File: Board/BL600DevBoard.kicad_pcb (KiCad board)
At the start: 2 copper layers, 42 parts, among them CN1 Socket_BL600, CON1 USB-MINI-B, P1 CONN_01X17, P2 CONN_BL600_SWDIF, P3 CONN_01X17, SW1 DIPSW_8, U1 93C56, U2 FT232H, U3 TC7SZ125, U4 TC7SZ125, X1 12M

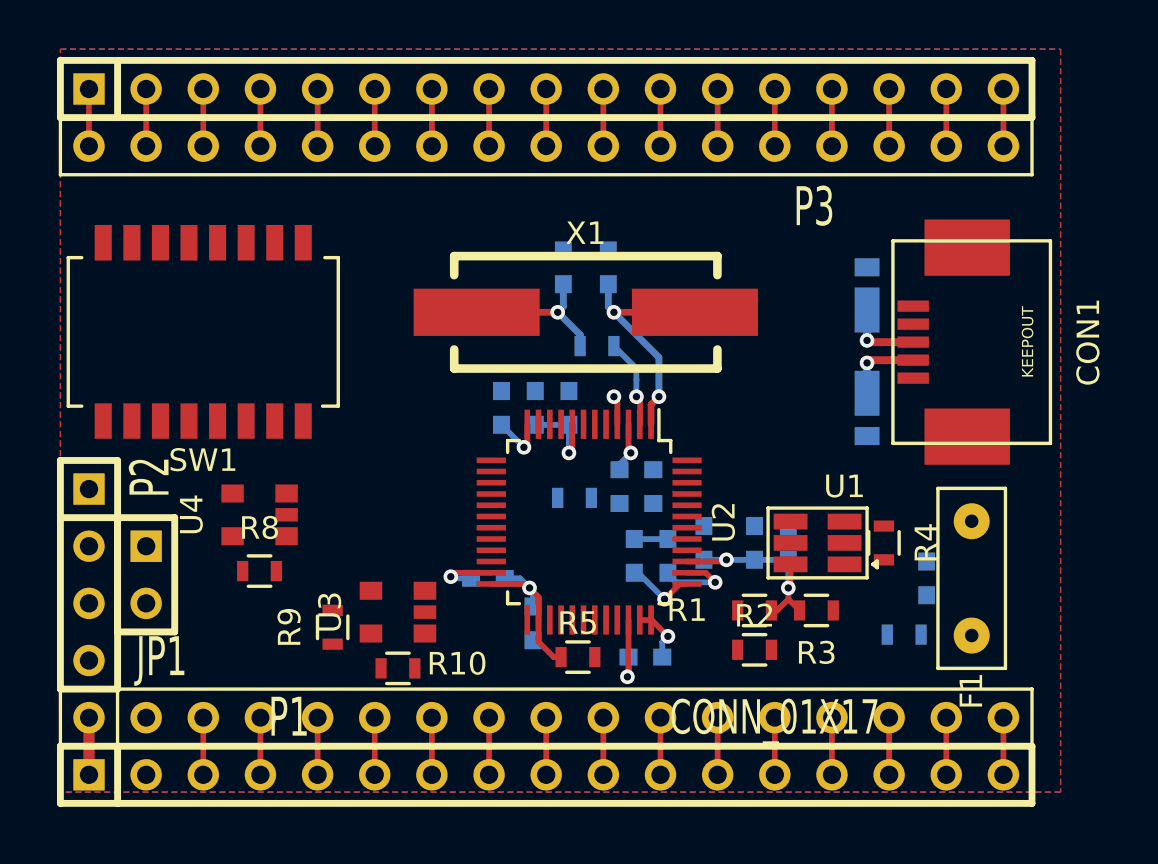
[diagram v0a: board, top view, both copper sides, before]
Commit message: Add panelized board cutting path data
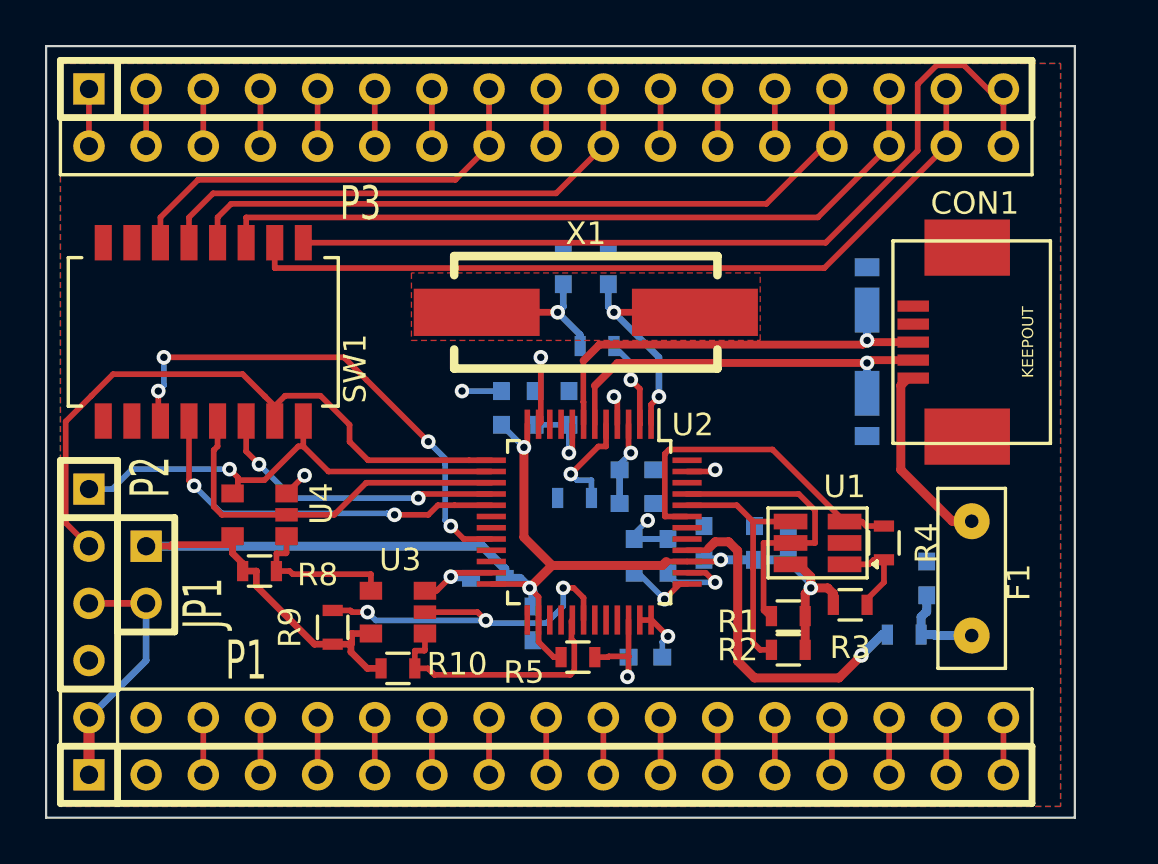
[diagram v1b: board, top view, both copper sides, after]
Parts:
- moved R1 1.52 mm to (184.8, 115.5)
- moved R3 1.52 mm to (187.5, 115.0)
- moved R2 1.50 mm to (184.8, 117.0)
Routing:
- net /VCC3.3: track 20.3 -> 69.9 mm
- net Net-(CN1-Pad18): track 2.54 -> 39.4 mm
- net Net-(CN1-Pad19): track 2.54 -> 35.8 mm
- net Net-(CN1-Pad20): track 2.54 -> 33.6 mm
- net Net-(CN1-Pad21): track 2.54 -> 32.4 mm
- net /SWDCLK_TxD: track 0.00 -> 28.9 mm
- net /RI#: track 0.00 -> 22.5 mm, vias 0 -> 4
- net /SWDIO_RxD: track 0.00 -> 21.4 mm, vias 0 -> 1
- net Net-(CN1-Pad25): track 2.54 -> 23.4 mm
- net Net-(CN1-Pad27): track 2.54 -> 19.6 mm
- net /TDO_RTS#: track 0.00 -> 17.0 mm
- net /DTR#: track 0.00 -> 16.9 mm, vias 0 -> 2
- net /SWDIO_OE: track 0.00 -> 16.5 mm, vias 0 -> 3
- net Net-(CON1-Pad3): track 3.43 -> 19.2 mm
- net Net-(FB1-Pad2): track 0.00 -> 15.2 mm, vias 0 -> 1
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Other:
- board outline added: 45.7 x 34.3 mm
- net class CLOCK: trace_width 0.3 -> 0.254
- net class POWER: trace_width 0.254 -> 0.35
- board text added: "BL600DevBoard Rev.A 20141112"

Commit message: TDI/TDO修正版に基板レイアウトを変更
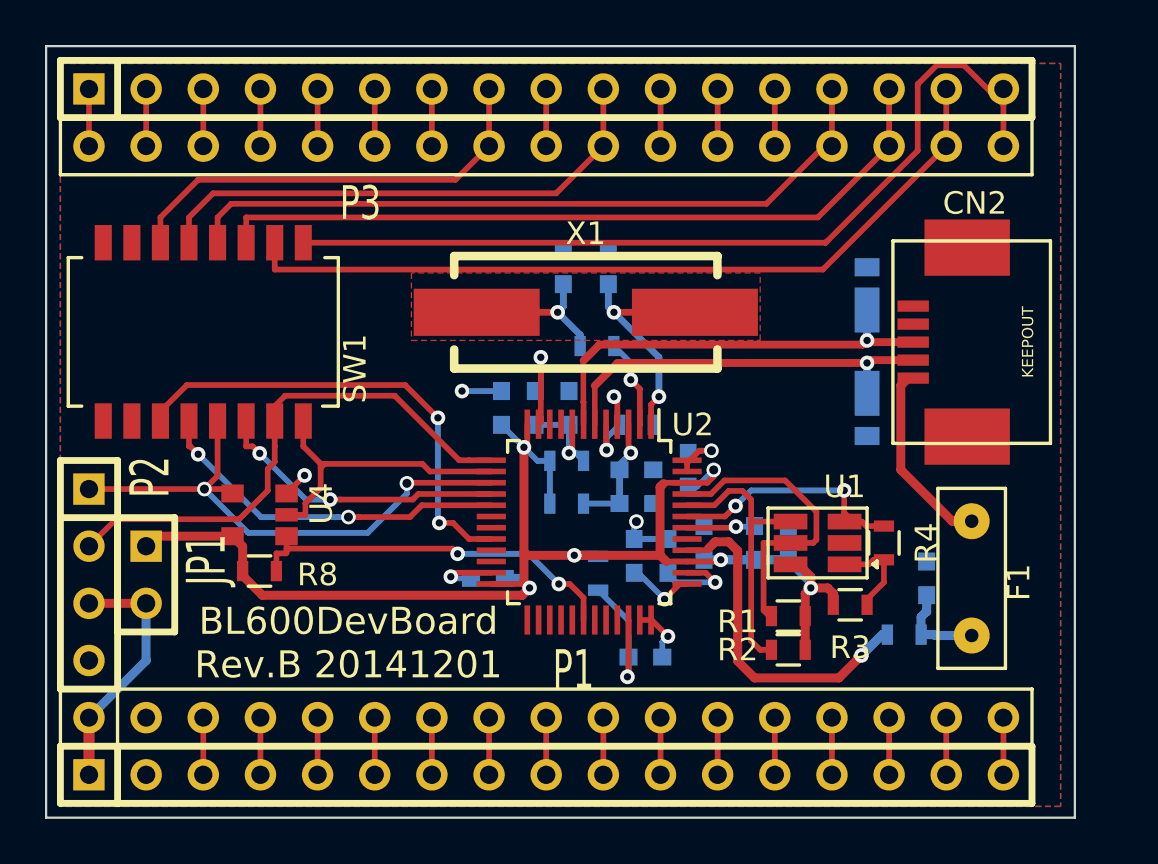
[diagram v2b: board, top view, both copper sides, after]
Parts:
- removed CON1: USB-MINI-B, AVR32Board:HIROSE_UX60SC-MB-5ST
- removed R10, R9: 10k, Resistors_SMD:R_0603
- removed U3: TC7SZ125, Housings_JEITA:SC-74A
- added CN2: USB-MINI-B, AVR32Board:HIROSE_UX60SC-MB-5ST, F.Cu at (196.4, 103.3)
- added FB2: 470/1A, Resistors_SMD:R_0603, B.Cu at (174.9, 108.6)
- added FB3: 470/1A, Resistors_SMD:R_0603, B.Cu at (174.9, 110.5)
- R5: moved to B.Cu
- moved C14 9.71 mm to (180.3, 109.0), turned to 270 degrees
- moved R7 4.26 mm to (178.0, 107.0), turned to 0 degrees
- moved R5 3.83 mm to (176.3, 113.6), turned to 90 degrees
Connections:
- P2 pad 1: /SWDIO_RxD -> /TDO_RTS#
- R8 pad 2: Net-(R8-Pad2) -> /SWDIO_OE
- SW1 pad 1: /SWDIO_RxD -> /TDI_RxD
- U2 pad 14: /SWDIO_RxD -> /TDI_RxD
- U2 pad 26: /VCC3.3 -> (no net)
- U2 pad 29: /SWDEN -> (no net)
- U2 pad 46: (no net) -> /VCC3.3
- U4 pad 1: Net-(R8-Pad2) -> /SWDIO_OE
- U4 pad 2: /TDO_RTS# -> /TDI_RxD
- U4 pad 4: /SWDIO_RxD -> /TDO_RTS#
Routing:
- net /SWDIO_RxD: track 21.4 -> 0.00 mm, vias 1 -> 0
- net /TDI_RxD: track 0.00 -> 13.4 mm
- net /SWDEN: track 11.6 -> 0.00 mm
- net /TDO_RTS#: track 17.0 -> 24.5 mm, vias 0 -> 2
- net Net-(R8-Pad2): track 6.98 -> 0.00 mm
- net /VCC3.3: track 69.9 -> 63.7 mm, vias 4 -> 6
- net /SWDCLK_TxD: track 28.9 -> 23.9 mm
- net Net-(R4-Pad1): track 15.0 -> 10.8 mm, vias 0 -> 2
- net Net-(R7-Pad1): track 4.88 -> 2.51 mm
- net Net-(C7-Pad1): track 4.96 -> 6.98 mm
- net GND: track 19.4 -> 21.2 mm, vias 8 -> 9
- net /VPHY: track 3.77 -> 5.37 mm
- net /RI#: track 22.5 -> 21.3 mm, vias 4 -> 2
- net Net-(R2-Pad1): track 11.2 -> 12.4 mm
- net /DTR#: track 16.9 -> 16.1 mm
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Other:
- board text added: "BL600DevBoard Rev.B 20141201"
- board text removed: "BL600DevBoard Rev.A 20141112"

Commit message: U4のリファレンスを欠番になっていたU3に変更。 ACBUS4経由でBL600のリセットを行えるように信号追加。
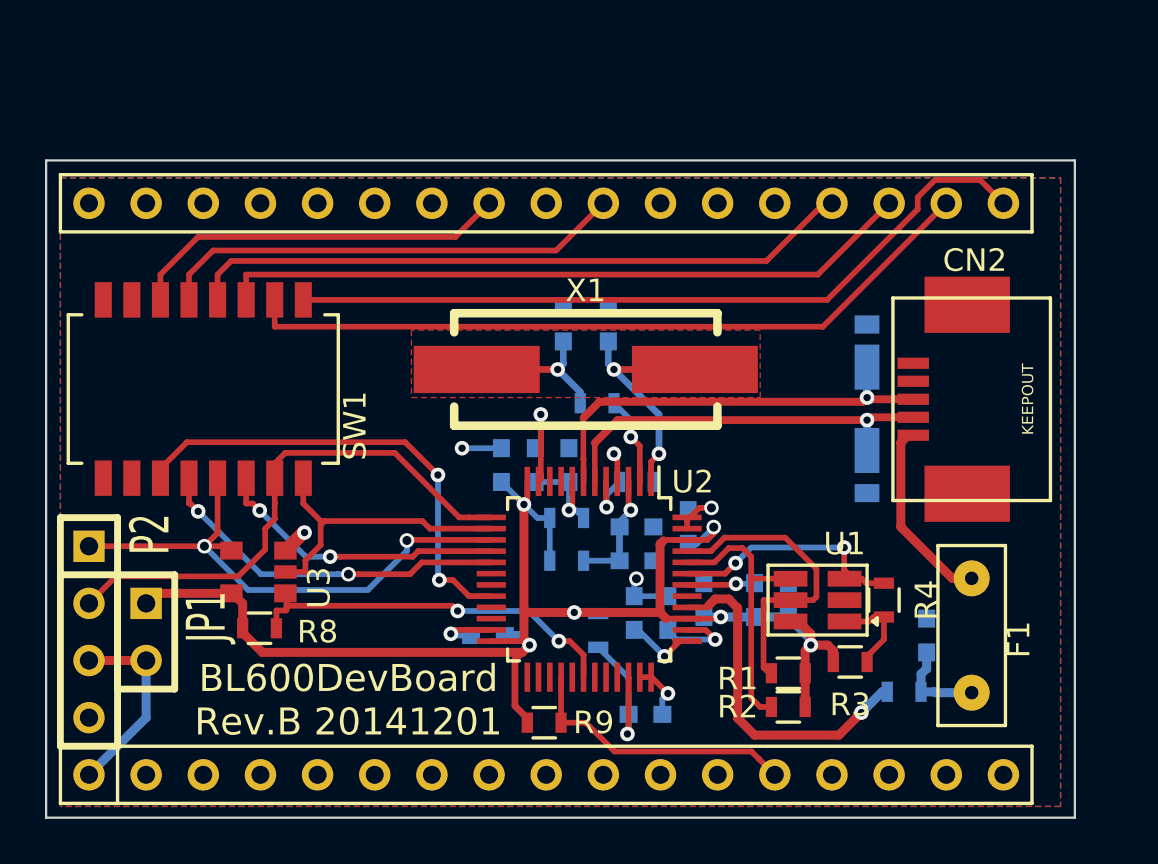
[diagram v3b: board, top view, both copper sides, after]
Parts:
- removed P1, P3: CONN_01X17, BL600:SIL-17
- removed U4: TC7SZ125, Housings_JEITA:SC-74A
- added R9: 10k, Resistors_SMD:R_0603, F.Cu at (173.9, 120.2)
- added U3: TC7SZ125, Housings_JEITA:SC-74A, F.Cu at (161.2, 113.5)
- moved C1 2.54 mm to (184.8, 114.8)
- moved C10 2.54 mm to (175.0, 108.8)
- moved C11 2.54 mm to (173.5, 108.8)
- moved C12 2.54 mm to (178.0, 111.5)
- moved C13 2.54 mm to (178.0, 113.0)
- moved C14 2.54 mm to (180.3, 111.5)
- moved C16 2.54 mm to (172.0, 108.8)
- moved C3 2.54 mm to (176.8, 102.5)
- moved C4 2.54 mm to (183.2, 114.8)
- moved C5 2.54 mm to (181.0, 114.8)
- moved C6 2.54 mm to (174.8, 102.5)
- moved CN1 2.54 mm to (196.8, 109.9)
- moved D1 2.54 mm to (188.2, 103.8)
- moved D2 2.54 mm to (188.2, 108.8)
- moved FB2 2.54 mm to (174.9, 111.1)
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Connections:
- U2 pad 28: (no net) -> Net-(CN1-Pad13)
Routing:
- net Net-(CN1-Pad13): track 2.54 -> 12.5 mm
- net Net-(CN1-Pad18): track 39.5 -> 34.1 mm
- net /VCC3.3: track 63.7 -> 67.6 mm
- net Net-(CN1-Pad9): track 2.54 -> 0.00 mm
- net Net-(CN1-Pad8): track 2.54 -> 0.00 mm
- net Net-(CN1-Pad7): track 2.54 -> 0.00 mm
- net Net-(CN1-Pad6): track 2.54 -> 0.00 mm
- net Net-(CN1-Pad5): track 2.54 -> 0.00 mm
- net Net-(CN1-Pad4): track 2.54 -> 0.00 mm
- net Net-(CN1-Pad3): track 2.54 -> 0.00 mm
- net Net-(CN1-Pad17): track 2.54 -> 0.00 mm
- net Net-(CN1-Pad16): track 2.54 -> 0.00 mm
- net Net-(CN1-Pad15): track 2.54 -> 0.00 mm
- net Net-(CN1-Pad14): track 2.54 -> 0.00 mm
- net Net-(CN1-Pad12): track 2.54 -> 0.00 mm
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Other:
- board size 45.7 x 34.3 mm -> 45.7 x 29.2 mm
